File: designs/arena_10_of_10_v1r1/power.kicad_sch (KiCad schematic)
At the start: 3 parts

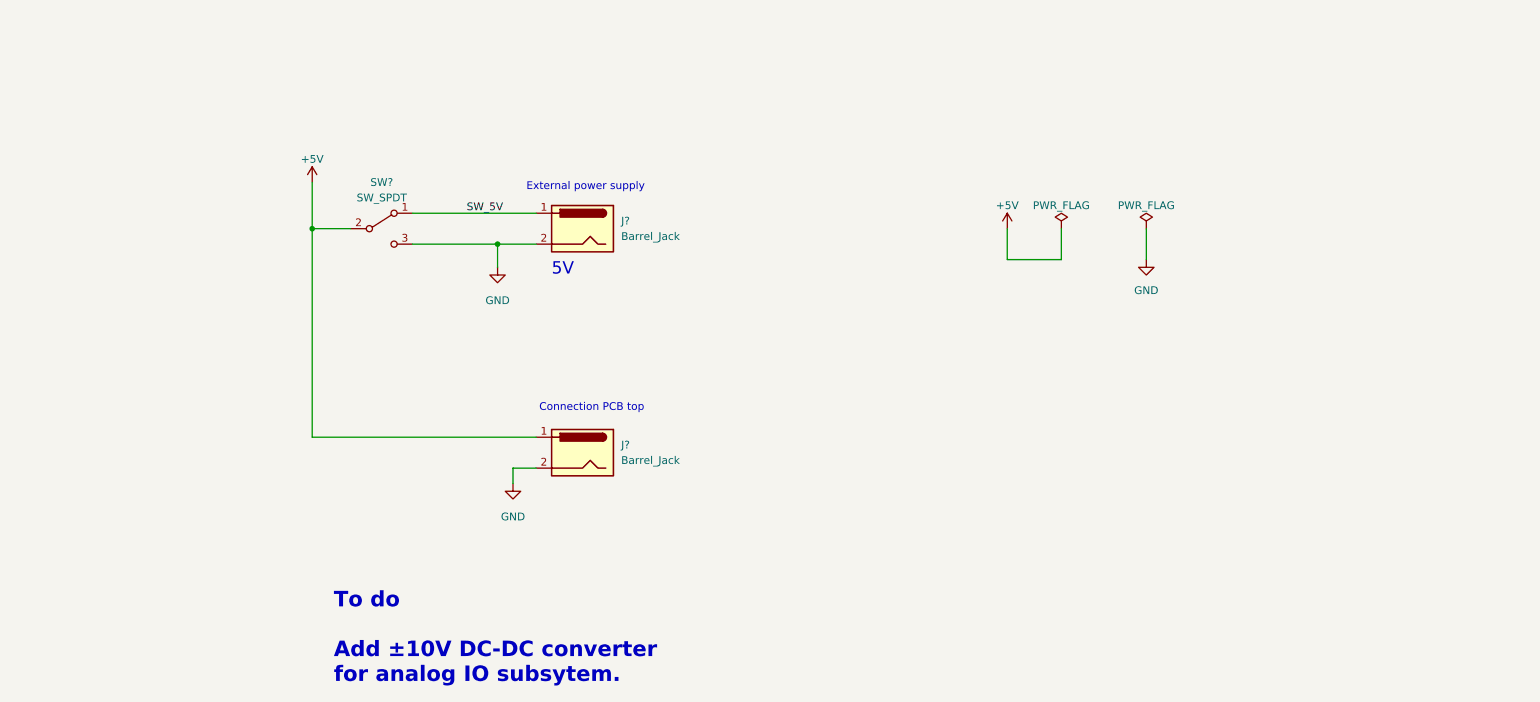
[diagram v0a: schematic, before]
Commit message: Fixed some issues with analog subsystem and added ethernet connection.
Added +/-15V power rails for bipolar analog inputs. Added 10V reference
voltage. Fixed connections for ethernet connection to teensy.
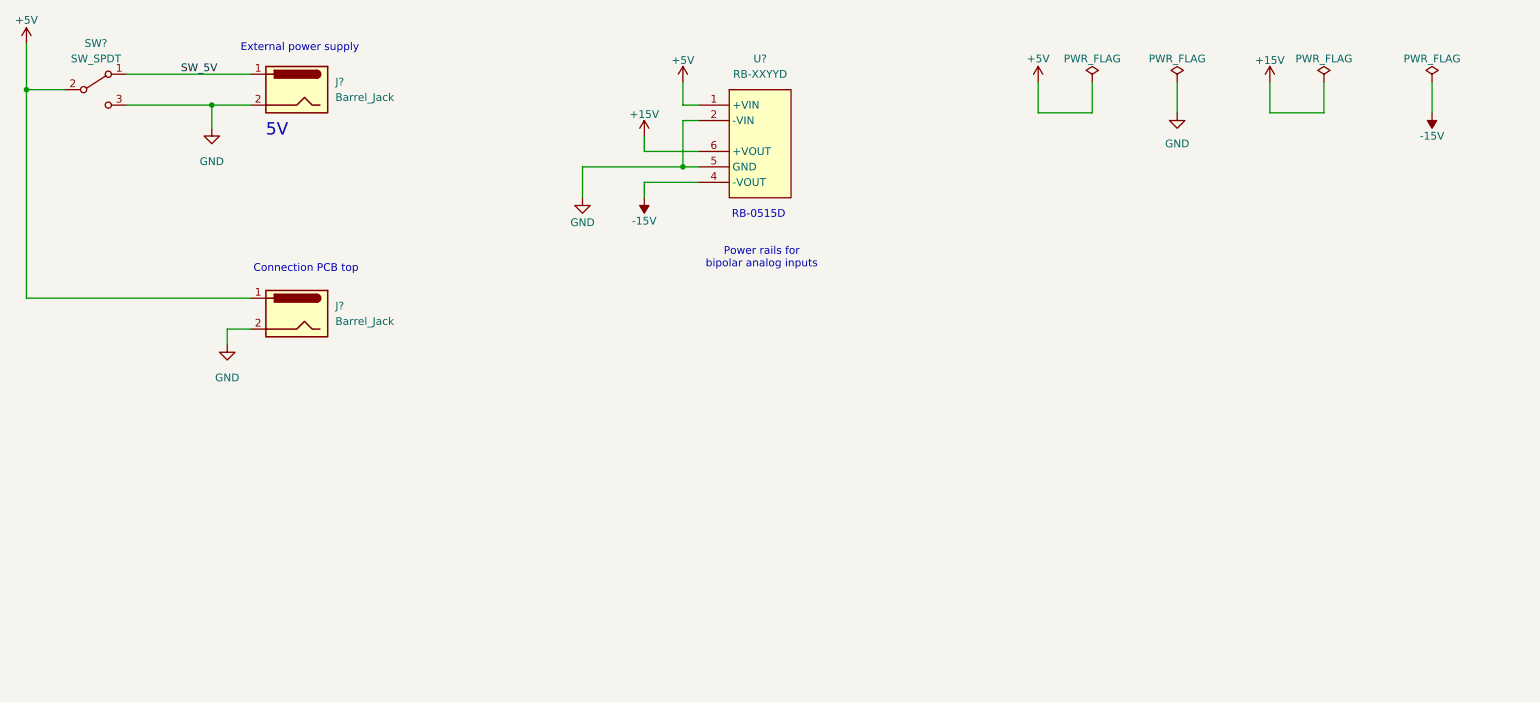
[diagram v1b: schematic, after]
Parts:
- added U?: RB-XXYYD, symbol recom_rbxxyyd:RB-XXYYD
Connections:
- net +5V: now also U?.1 (+VIN)
- net GND: now also U?.2 (-VIN), U?.5 (GND)
- new net +15V: U?.6 (+VOUT)
- new net -15V: U?.4 (-VOUT)
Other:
- note added: "Power rails for bipolar analog inputs"
- note added: "RB-0515D"
- note removed: "To do Add ±10V DC-DC converter for analog IO subsytem."
- moved on the sheet: J?, SW?

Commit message: Added initial annotation.
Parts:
- gave numbers to parts that had none: 4
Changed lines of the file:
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@@
 		(on_board yes)
 		(dnp no)
-		(property "Reference" "#PWR0423"
+		(property "Reference" "#PWR0283"
 			(at 124.46 55.88 0)
 			(effects
@@
 			(project "arena_10_of_10_v1r1"
 				(path "/056666d2-2c8f-491c-bcad-db3c517779a8/f8e525f6-92ff-481c-b9d6-983b91f2917d"
-					(reference "#PWR0423")
+					(reference "#PWR0283")
 					(unit 1)
 				)
@@
 		(on_board yes)
 		(dnp no)
-		(property "Reference" "#PWR0425"
+		(property "Reference" "#PWR0284"
 			(at 134.62 43.18 0)
 			(effects
@@
 			(project ""
 				(path "/056666d2-2c8f-491c-bcad-db3c517779a8/f8e525f6-92ff-481c-b9d6-983b91f2917d"
-					(reference "#PWR0425")
+					(reference "#PWR0284")
 					(unit 1)
 				)
@@
 		(on_board yes)
 		(dnp no)
-		(property "Reference" "#PWR0342"
+		(property "Reference" "#PWR0287"
 			(at 199.39 34.29 0)
 			(effects
@@
 			(project "arena_10_of_10_v1r1"
 				(path "/056666d2-2c8f-491c-bcad-db3c517779a8/f8e525f6-92ff-481c-b9d6-983b91f2917d"
-					(reference "#PWR0342")
+					(reference "#PWR0287")
 					(unit 1)
 				)
@@
 		(dnp no)
 		(fields_autoplaced yes)
-		(property "Reference" "#PWR0343"
+		(property "Reference" "#PWR0288"
 			(at 222.25 41.91 0)
 			(effects
@@
 			(project "arena_10_of_10_v1r1"
 				(path "/056666d2-2c8f-491c-bcad-db3c517779a8/f8e525f6-92ff-481c-b9d6-983b91f2917d"
-					(reference "#PWR0343")
+					(reference "#PWR0288")
 					(unit 1)
 				)
@@
 		(on_board yes)
 		(dnp no)
-		(property "Reference" "#PWR0441"
+		(property "Reference" "#PWR0290"
 			(at 264.16 31.75 0)
 			(effects
@@
 			(project "arena_10_of_10_v1r1"
 				(path "/056666d2-2c8f-491c-bcad-db3c517779a8/f8e525f6-92ff-481c-b9d6-983b91f2917d"
-					(reference "#PWR0441")
+					(reference "#PWR0290")
 					(unit 1)
 				)
@@
 		(dnp no)
 		(fields_autoplaced yes)
-		(property "Reference" "J?"
+		(property "Reference" "J25"
 			(at 83.82 30.4799 0)
 			(effects
@@
 			(project "arena_10_of_10_v1r1"
 				(path "/056666d2-2c8f-491c-bcad-db3c517779a8/f8e525f6-92ff-481c-b9d6-983b91f2917d"
-					(reference "J?")
+					(reference "J25")
 					(unit 1)
 				)
@@
 		(dnp no)
 		(fields_autoplaced yes)
-		(property "Reference" "SW?"
+		(property "Reference" "SW1"
 			(at 44.45 24.13 0)
 			(effects
@@
 			(project "arena_10_of_10_v1r1"
 				(path "/056666d2-2c8f-491c-bcad-db3c517779a8/f8e525f6-92ff-481c-b9d6-983b91f2917d"
-					(reference "SW?")
+					(reference "SW1")
 					(unit 1)
 				)
@@
 		(dnp no)
 		(fields_autoplaced yes)
-		(property "Reference" "#PWR0341"
+		(property "Reference" "#PWR0281"
 			(at 63.5 44.45 0)
 			(effects
@@
 			(project "arena_10_of_10_v1r1"
 				(path "/056666d2-2c8f-491c-bcad-db3c517779a8/f8e525f6-92ff-481c-b9d6-983b91f2917d"
-					(reference "#PWR0341")
+					(reference "#PWR0281")
 					(unit 1)
 				)
@@
 		(on_board yes)
 		(dnp no)
-		(property "Reference" "#FLG02"
+		(property "Reference" "#FLG03"
 			(at 246.38 28.575 0)
 			(effects
@@
 			(project "arena_10_of_10_v1r1"
 				(path "/056666d2-2c8f-491c-bcad-db3c517779a8/f8e525f6-92ff-481c-b9d6-983b91f2917d"
-					(reference "#FLG02")
+					(reference "#FLG03")
 					(unit 1)
 				)
@@
 		(on_board yes)
 		(dnp no)
-		(property "Reference" "#PWR0426"
+		(property "Reference" "#PWR0285"
 			(at 134.62 45.72 0)
 			(effects
@@
 			(project ""
 				(path "/056666d2-2c8f-491c-bcad-db3c517779a8/f8e525f6-92ff-481c-b9d6-983b91f2917d"
-					(reference "#PWR0426")
+					(reference "#PWR0285")
 					(unit 1)
 				)
@@
 		(dnp no)
 		(fields_autoplaced yes)
-		(property "Reference" "#FLG03"
+		(property "Reference" "#FLG02"
 			(at 222.25 28.575 0)
 			(effects
@@
 			(project "arena_10_of_10_v1r1"
 				(path "/056666d2-2c8f-491c-bcad-db3c517779a8/f8e525f6-92ff-481c-b9d6-983b91f2917d"
-					(reference "#FLG03")
+					(reference "#FLG02")
 					(unit 1)
 				)
@@
 		(on_board yes)
 		(dnp no)
-		(property "Reference" "#PWR0424"
+		(property "Reference" "#PWR0286"
 			(at 140.97 34.29 0)
 			(effects
@@
 			(project ""
 				(path "/056666d2-2c8f-491c-bcad-db3c517779a8/f8e525f6-92ff-481c-b9d6-983b91f2917d"
-					(reference "#PWR0424")
+					(reference "#PWR0286")
 					(unit 1)
 				)
@@
 		(dnp no)
 		(fields_autoplaced yes)
-		(property "Reference" "#PWR0561"
+		(property "Reference" "#PWR0282"
 			(at 66.04 80.01 0)
 			(effects
@@
 			(project "arena_10_of_10_v1r1"
 				(path "/056666d2-2c8f-491c-bcad-db3c517779a8/f8e525f6-92ff-481c-b9d6-983b91f2917d"
-					(reference "#PWR0561")
+					(reference "#PWR0282")
 					(unit 1)
 				)
@@
 		(on_board yes)
 		(dnp no)
-		(property "Reference" "U?"
+		(property "Reference" "U82"
 			(at 153.67 26.67 0)
 			(effects
@@
 			(project ""
 				(path "/056666d2-2c8f-491c-bcad-db3c517779a8/f8e525f6-92ff-481c-b9d6-983b91f2917d"
-					(reference "U?")
+					(reference "U82")
 					(unit 1)
 				)
@@
 		(on_board yes)
 		(dnp no)
-		(property "Reference" "#PWR0440"
+		(property "Reference" "#PWR0289"
 			(at 237.49 34.29 0)
 			(effects
@@
 			(project "arena_10_of_10_v1r1"
 				(path "/056666d2-2c8f-491c-bcad-db3c517779a8/f8e525f6-92ff-481c-b9d6-983b91f2917d"
-					(reference "#PWR0440")
+					(reference "#PWR0289")
 					(unit 1)
 				)
@@
 		(on_board yes)
 		(dnp no)
-		(property "Reference" "#PWR0340"
+		(property "Reference" "#PWR0280"
 			(at 33.02 27.94 0)
 			(effects
@@
 			(project "arena_10_of_10_v1r1"
 				(path "/056666d2-2c8f-491c-bcad-db3c517779a8/f8e525f6-92ff-481c-b9d6-983b91f2917d"
-					(reference "#PWR0340")
+					(reference "#PWR0280")
 					(unit 1)
 				)
@@
 		(dnp no)
 		(fields_autoplaced yes)
-		(property "Reference" "J?"
+		(property "Reference" "J26"
 			(at 83.82 67.3099 0)
 			(effects
@@
 			(project "arena_10_of_10_v1r1"
 				(path "/056666d2-2c8f-491c-bcad-db3c517779a8/f8e525f6-92ff-481c-b9d6-983b91f2917d"
-					(reference "J?")
-					(unit 1)
-				)
+					(reference "J26")
+					(unit 1)
+				)

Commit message: Finished footprint assignment.
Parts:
- U82: footprint (none) -> RB-XXYYD:RB-XXYYYD
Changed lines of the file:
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@@
 			)
 		)
-		(property "Footprint" ""
+		(property "Footprint" "RB-XXYYD:RB-XXYYYD"
 			(at 153.67 40.64 0)
 			(effects

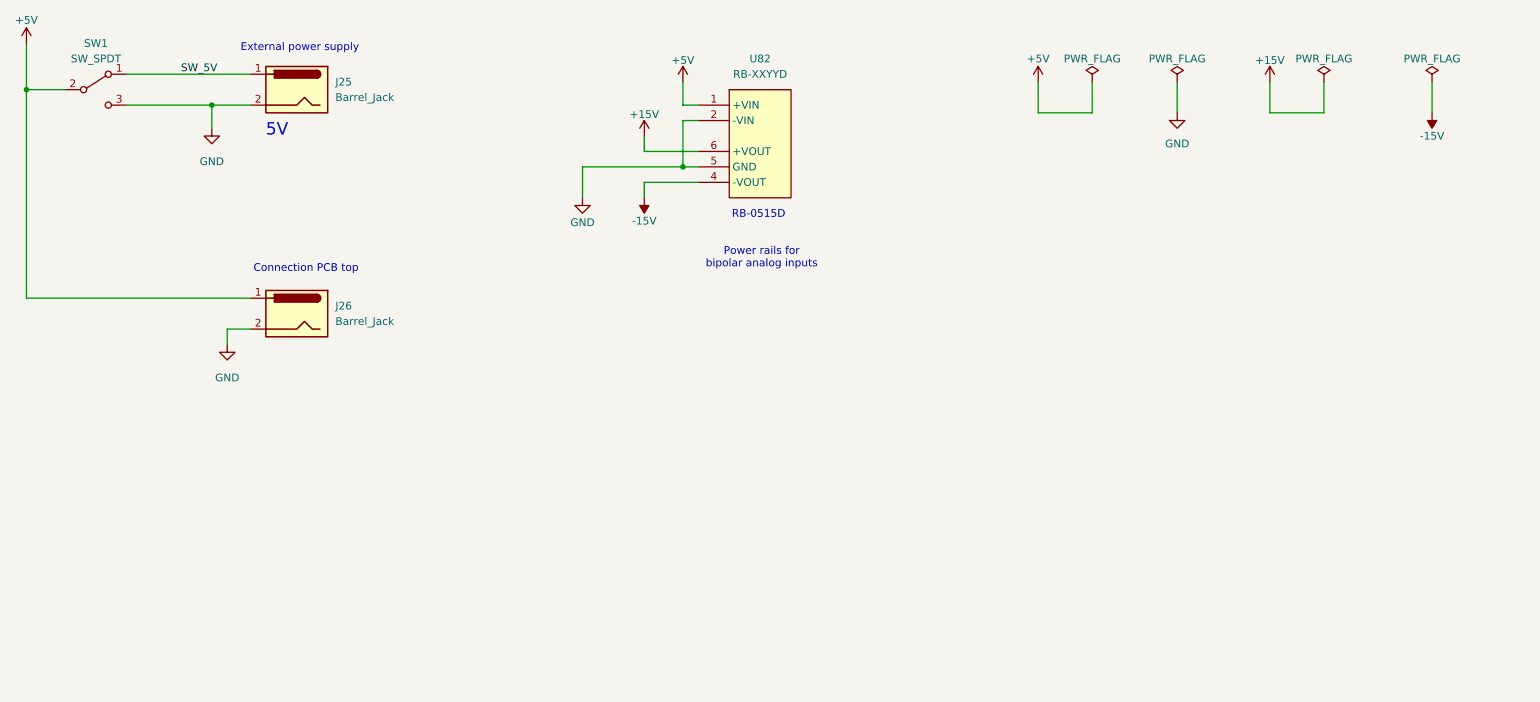
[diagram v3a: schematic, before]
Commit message: Working through schematic design rule check.
Just some power issues remaing.
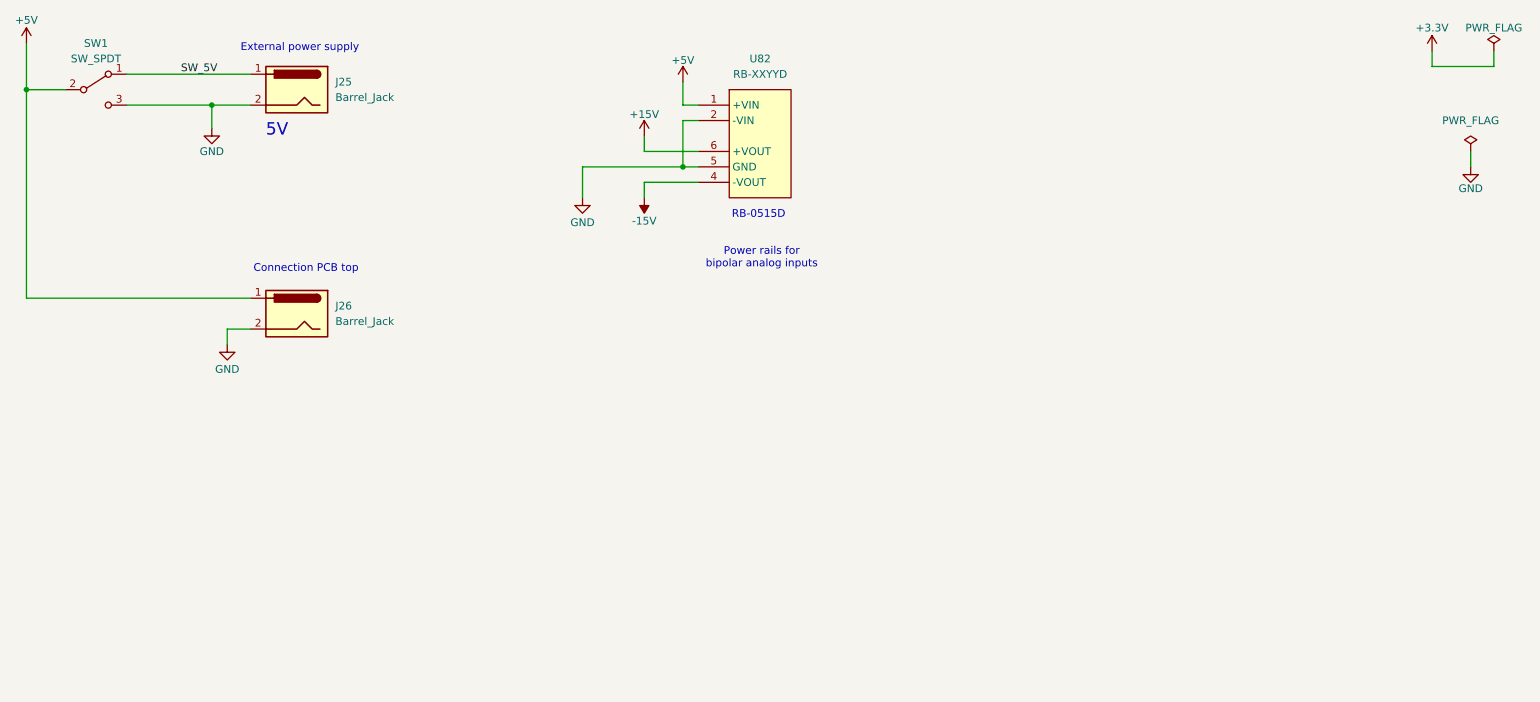
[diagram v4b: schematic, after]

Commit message: Resolved all DSR voilations in schematic.
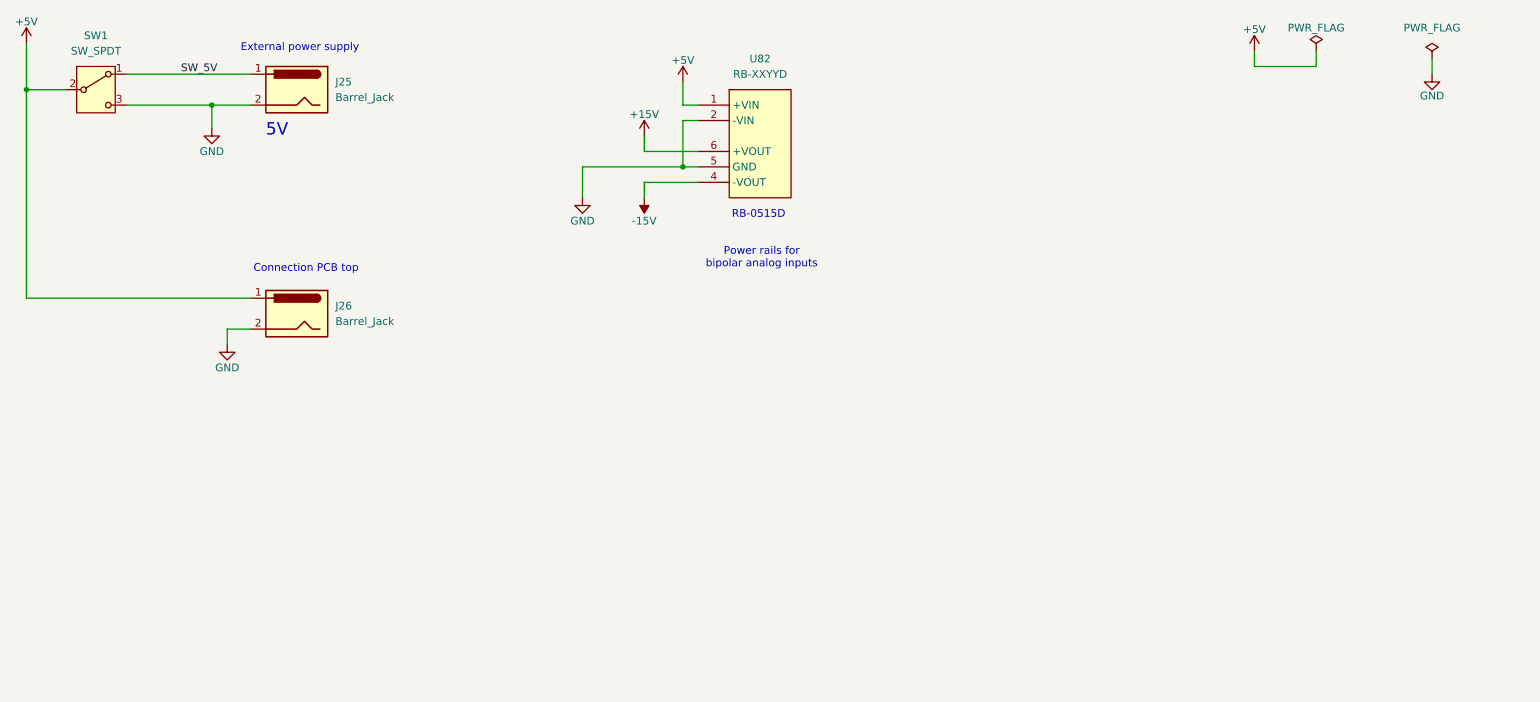
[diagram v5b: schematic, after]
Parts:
- J25, J26: footprint arena_custom:DCJACK_2PIN_HIGHCURRENT -> (none)
- SW1: footprint arena_custom:slide_switch -> (none)

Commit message: Worked on automatic layout of panels + conditioning components.
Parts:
- J25, J26: footprint (none) -> arena_custom:DCJACK_2PIN_HIGHCURRENT
- SW1: footprint (none) -> arena_custom:slide_switch
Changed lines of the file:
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@@
 			)
 		)
-		(property "Footprint" ""
+		(property "Footprint" "arena_custom:DCJACK_2PIN_HIGHCURRENT"
 			(at 76.2 69.596 0)
 			(effects
@@
 			)
 		)
-		(property "Footprint" ""
+		(property "Footprint" "arena_custom:DCJACK_2PIN_HIGHCURRENT"
 			(at 76.2 32.766 0)
 			(effects
@@
 			)
 		)
-		(property "Footprint" ""
+		(property "Footprint" "arena_custom:slide_switch"
 			(at 44.45 31.75 0)
 			(effects
